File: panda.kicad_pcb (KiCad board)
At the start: 2 copper layers, 100 x 125 mm, 158 parts, among them J1 PIN6-9_Breakout, J10 Screw_Terminal_01x02, J11 24V_Lockout_Key_Switch, J12 XT60-M, J13 PT_1, J14 PT_4, J15 PT_2, J16 PT_5, J17 PT_3, J18 PT_6, J19 4-Pin Load Cell, J2 PIN10-13_Breakout, J20 5-Pin Load Cell, J21 Ignitor Screw Terminal, J3 Valve_1_PWR, J4 Valve_4_PWR, J5 Valve_2_PWR, J6 Valve_5_PWR, J7 Valve_3_PWR, J8 Valve_6_PWR, J9 Screw_Terminal_01x03, K1 G5Q-1A DC24, K2 G5Q-1A DC24, Q1 BSS138, Q2 BSS138, Q3 BSS138, Q4 BSS138, Q5 BSS138, Q6 BSS138, Q7 BSS138, Q8 BSS138, U1 ESP32-S3, U2 ADS112C04, U3 ADS112C04, U4 ADS112C04, U5 ADS112C04, U6 XC6206P332MR, U8 TPS5430DDA, U9 INA199A2DCK

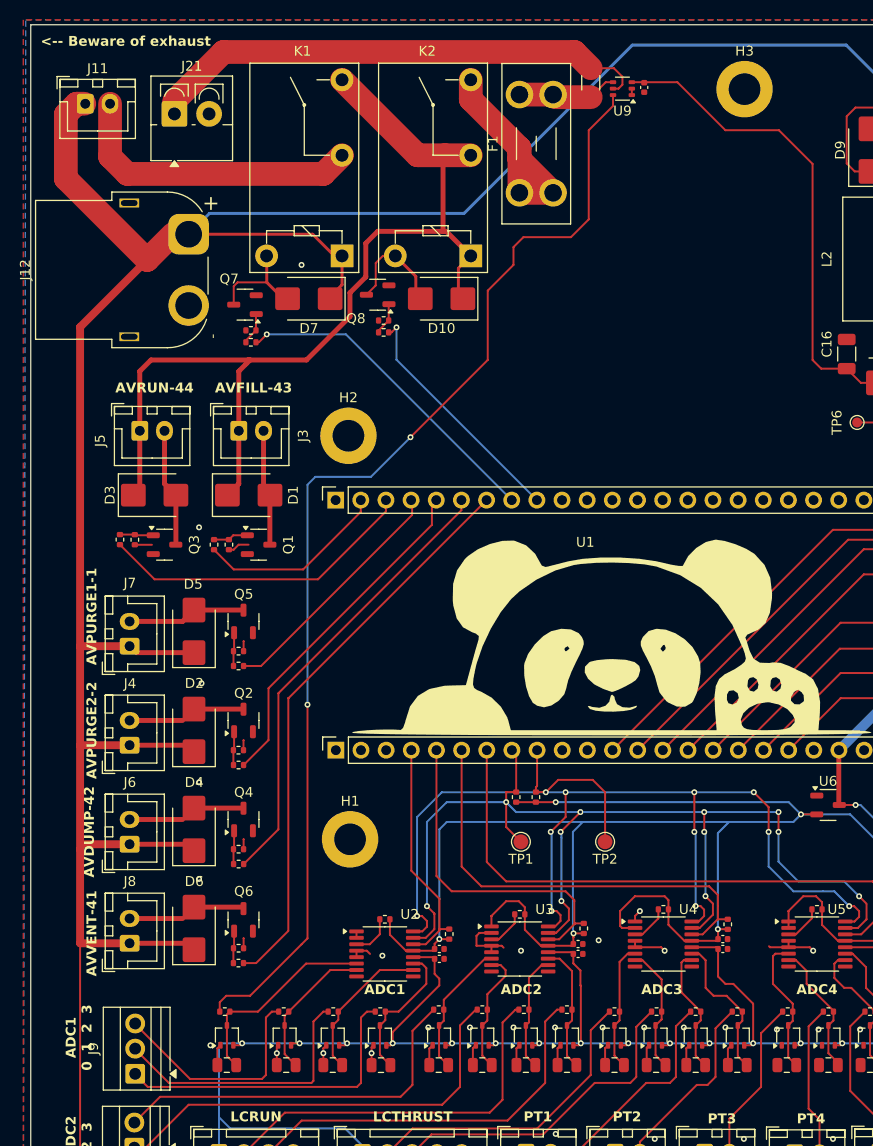
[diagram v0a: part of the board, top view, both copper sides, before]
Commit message: Add indicator LEDs and digital +24VSafe detection line
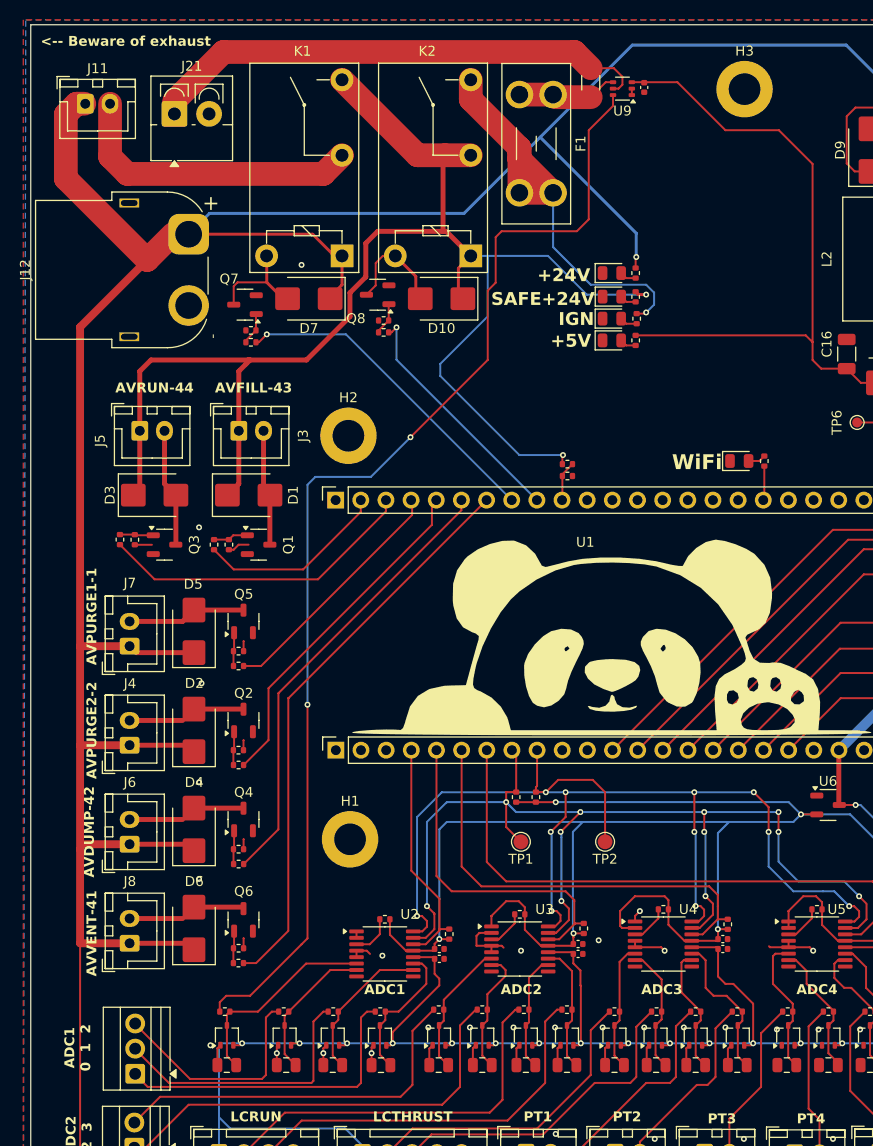
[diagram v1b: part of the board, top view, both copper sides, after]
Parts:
- added D11: LED-G, LED_SMD:LED_0805_2012Metric, F.Cu at (168.9, 56.6)
- added D12: LED-G, LED_SMD:LED_0805_2012Metric, F.Cu at (168.9, 49.8)
- added D13: LED-G, LED_SMD:LED_0805_2012Metric, F.Cu at (168.9, 52.2)
- added D14: LED-G, LED_SMD:LED_0805_2012Metric, F.Cu at (168.9, 54.4)
- added D8: LED-Y, LED_SMD:LED_0805_2012Metric, F.Cu at (181.8, 68.8)
- added R55: 1k, Resistor_SMD:R_0402_1005Metric, F.Cu at (184.3, 68.8)
- added R56: 1k, Resistor_SMD:R_0402_1005Metric, F.Cu at (171.3, 56.6)
- added R57: 22k, Resistor_SMD:R_0402_1005Metric, F.Cu at (171.3, 49.8)
- added R58: 22k, Resistor_SMD:R_0402_1005Metric, F.Cu at (171.3, 52.2)
- added R59: 22k, Resistor_SMD:R_0402_1005Metric, F.Cu at (171.4, 54.4)
- added R60: 270k, Resistor_SMD:R_0402_1005Metric, F.Cu at (164.4, 69.1)
- added R61: 33k, Resistor_SMD:R_0402_1005Metric, F.Cu at (164.4, 70.3)
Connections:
- net /Ignitor Control/IGNITOR_SOURCE renamed /Ignitor Control/IGNITOR_+VE
- net Net-(F1-Pad1) renamed /Ignitor Control/IGN_SUPPLY
- U1 pad 21: unconnected-(U1-GPIO21-Pad21) -> /ESP32 Breakout/WIFI_INDICATOR
- U1 pad 38: unconnected-(U1-GPIO38-Pad38) -> /ESP32 Breakout/+24V_SAFE_DETECT
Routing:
- net +24V_SAFE: track 100.0 -> 151.3 mm, vias 0 -> 2
- net /Ignitor Control/IGN_SUPPLY: track 22.8 -> 43.7 mm, vias 0 -> 1
- net +5V: track 320.5 -> 338.7 mm
- net +24V: track 422.0 -> 439.3 mm, vias 1 -> 2
- net /ESP32 Breakout/+24V_SAFE_DETECT: track 0.00 -> 4.07 mm
- net /ESP32 Breakout/WIFI_INDICATOR: track 0.00 -> 3.47 mm
- net Net-(D8-A): track 0.00 -> 1.80 mm
- net Net-(D14-A): track 0.00 -> 1.78 mm
- net Net-(D13-A): track 0.00 -> 1.68 mm
- net Net-(D11-A): track 0.00 -> 1.67 mm
- net Net-(D12-A): track 0.00 -> 1.67 mm
- net IGN_Current_Measurement: track 116.5 -> 118.1 mm
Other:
- board text added: "+24V"
- board text added: "+5V"
- board text added: "ADC1 0 1 2"
- board text added: "IGN"
- board text added: "SAFE+24V"
- board text added: "WiFi"
- board text added: "https://github.com/Queens-Rocket-Engineering-Team/prop-panda"
- board text removed: "ADC1 0 1 2 3"

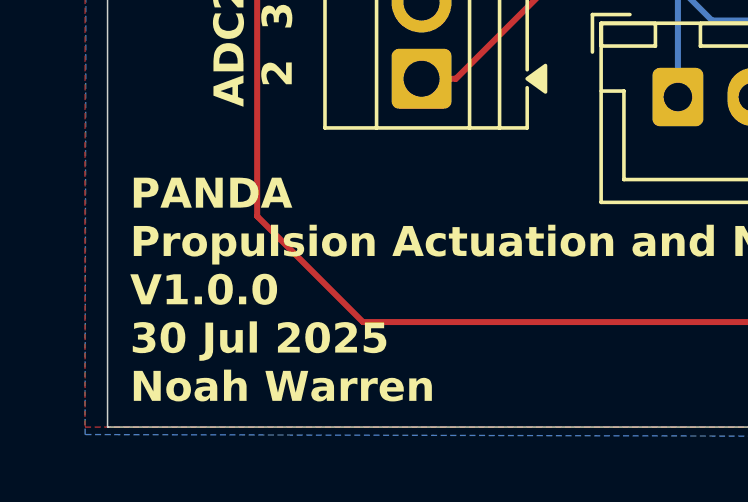
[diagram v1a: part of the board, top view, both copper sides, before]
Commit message: Update version numbers
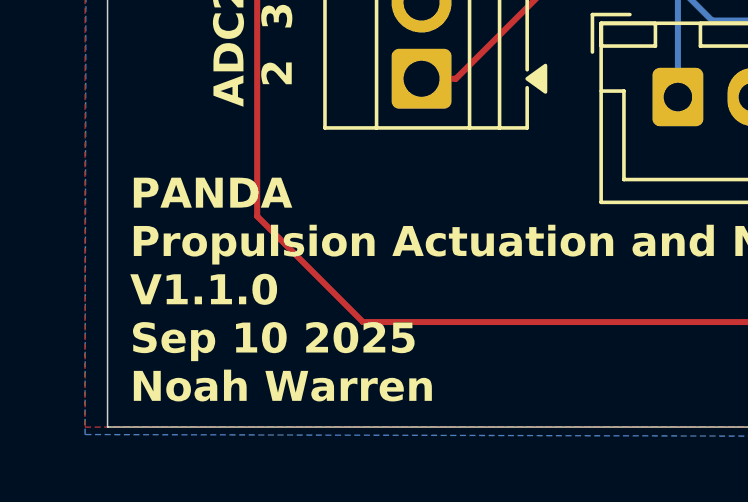
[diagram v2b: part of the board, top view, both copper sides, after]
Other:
- board text added: "PANDA Propulsion Actuation and Nominal Data Acquisition V1.1.0 Sep 10 2025 Noah Warren"
- board text removed: "PANDA Propulsion Actuation and Nominal Data Acquisition V1.0.0 30 Jul 2025 Noah Warren"
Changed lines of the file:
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@@
 	(title_block
 		(title "PANDA")
-		(rev "1.0.0")
+		(rev "1.1.0")
 		(company "Queen's Rocket Engineering Team")
-		(comment 1 "Propulsion Actuation and Nonsensical Data Acquisition")
+		(comment 1 "Propulsion Actuation and Nominal Data Acquisition")
 	)
 	(layers
@@
 		)
 	)
-	(gr_text "PANDA\nPropulsion Actuation and Nominal Data Acquisition\nV1.0.0\n30 Jul 2025\nNoah Warren"
+	(gr_text "PANDA\nPropulsion Actuation and Nominal Data Acquisition\nV1.1.0\nSep 10 2025\nNoah Warren"
 		(at 111 149 0)
 		(layer "F.SilkS")

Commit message: connected to GPIO pins
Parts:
- removed the U6 at (190.8, 103.5)
- added C1: 10uF, Capacitor_SMD:C_1206_3216Metric, F.Cu at (216.0, 92.0)
- added C15: 10uF, Capacitor_SMD:C_1206_3216Metric, F.Cu at (263.8, 51.6)
- added C16: 10uF, Capacitor_SMD:C_1206_3216Metric, F.Cu at (249.8, 59.5)
- added C18: 10uF, Capacitor_SMD:C_1206_3216Metric, F.Cu at (251.2, 54.5)
- added C2: 0.1μF, Capacitor_SMD:C_0402_1005Metric, F.Cu at (205.4, 93.4)
- added C20: 0.1μF, Capacitor_SMD:C_0402_1005Metric, F.Cu at (279.3, 45.2)
- added C3: 1μF, Capacitor_SMD:C_0402_1005Metric, F.Cu at (228.0, 87.5)
- added C4: 0.1μF, Capacitor_SMD:C_0402_1005Metric, F.Cu at (229.2, 90.0)
- added C5: 0.1μF, Capacitor_SMD:C_0402_1005Metric, F.Cu at (205.4, 99.3)
- added CR1: USBLC6-2SC6, Package_TO_SOT_SMD:SOT-23-6, F.Cu at (216.4, 71.5)
- added D11: 1N5819HW-7-F, Diode_SMD:D_SOD-123, F.Cu at (270.5, 77.1)
- added D12: 1N5819HW-7-F, Diode_SMD:D_SOD-123, F.Cu at (270.5, 82.8)
- added D14: LED-G, LED_SMD:LED_0805_2012Metric, F.Cu at (255.0, 60.0)
- added J1: USB_C_Receptacle_USB2.0_16P, Connector_USB:USB_C_Receptacle_HCTL_HC-TYPE-C-16P-01A, F.Cu at (225.0, 71.5)
- added R1: 0k, Resistor_SMD:R_0402_1005Metric, F.Cu at (202.0, 90.8)
- added R2: 10k, Resistor_SMD:R_0402_1005Metric, F.Cu at (202.5, 95.4)
- added R3: 5.1k, Resistor_SMD:R_0402_1005Metric, F.Cu at (219.2, 74.0)
- added R36: 680, Resistor_SMD:R_0402_1005Metric, F.Cu at (278.3, 37.2)
- added R4: 5.1k, Resistor_SMD:R_0402_1005Metric, F.Cu at (219.2, 69.0)
- added SW1: PTS636SM43SMTR LFS, Button_Switch_SMD:SW_Tactile_SPST_NO_Straight_CK_PTS636Sx25SMTRLFS, F.Cu at (195.8, 95.0)
- added SW2: PTS636SM43SMTR LFS, Button_Switch_SMD:SW_Tactile_SPST_NO_Straight_CK_PTS636Sx25SMTRLFS, F.Cu at (195.8, 100.2)
- added U7: XC6220B331PR-G, Package_TO_SOT_SMD:SOT-89-5, F.Cu at (260.6, 77.8)
- U1: value ESP32-S3 -> ESP32-S3-WROOM-1; footprint Library:ESP32_Devkit_C1_Noah -> RF_Module:ESP32-S3-WROOM-1
- moved G*** 127.9 mm to (41.1, 83.1)
- moved R8 76.2 mm to (239.2, 54.8)
- moved R9 75.9 mm to (239.2, 57.2)
- moved U1 60.1 mm to (216.2, 49.8), turned to 0 degrees
- moved C23 41.3 mm to (88.8, 132.3)
- moved C24 41.3 mm to (104.4, 132.3)
- moved C27 41.3 mm to (94.8, 132.3)
- moved D17 41.3 mm to (110.5, 54.9)
- moved D20 41.3 mm to (110.2, 129.3)
- moved H2 41.3 mm to (101.1, 68.8)
- moved Q2 41.3 mm to (90.5, 97.5)
- moved Q4 41.3 mm to (90.5, 107.5)
- moved Q5 41.3 mm to (90.5, 87.5)
- moved Q6 41.3 mm to (90.5, 117.6)
- moved R11 41.3 mm to (90.0, 102.0)
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- renumbered C5 to C10, C6 to C11, C7 to C12, C8 to C13, C10 to C14, C12 to C17, C14 to C19, C16 to C21, C29 to C22, C9 to C23, C13 to C24, C17 to C25, C18 to C26, C11 to C27, C15 to C28, C19 to C29, C20 to C30, C21 to C31, C22 to C32, C25 to C33, C26 to C34, C23 to C35, C24 to C36, C27 to C37, C28 to C38, C1 to C6, C2 to C7, C3 to C8, C4 to C9, D8 to D1, D7 to D10, D9 to D13, D11 to D15, D14 to D16, D10 to D17, D26 to D18, D28 to D19, D1 to D2, D34 to D20, D35 to D21, D27 to D22, D29 to D23, D36 to D24, D37 to D25, D30 to D26, D31 to D27, D38 to D28, D39 to D29, D2 to D3, D32 to D30, D33 to D31, D40 to D32, D41 to D33, D3 to D4, D4 to D5, D5 to D6, D6 to D7, D13 to D8, D12 to D9, J11 to J10, J12 to J11, J13 to J12, J14 to J13, J15 to J14, J16 to J15, J17 to J16, J18 to J17, J19 to J18, J20 to J19, J21 to J20, J9 to J21, J10 to J22, J1 to J3, J3 to J4, J4 to J5, J5 to J6, J6 to J7, J7 to J8, J8 to J9, L2 to L1, R3 to R10, R4 to R11, R5 to R12, R6 to R13, R7 to R14, R8 to R15, R9 to R16, R10 to R17, R11 to R18, R12 to R19, R13 to R20, R14 to R21, R15 to R22, R16 to R23, R17 to R24, R18 to R25, R19 to R26, R20 to R27, R21 to R28, R22 to R29, R23 to R30, R24 to R31, R58 to R32, R57 to R33, R25 to R34, R26 to R35, R29 to R37, R30 to R38, R56 to R39, R31 to R40, R32 to R41, R33 to R42, R34 to R43, R35 to R44, R36 to R45, R54 to R46, R59 to R47, R37 to R48, R38 to R49, R1 to R5, R53 to R50, R27 to R51, R28 to R52, R39 to R53, R40 to R54, R41 to R55, R42 to R56, R43 to R57, R44 to R58, R45 to R59, R2 to R6, R46 to R60, R47 to R61, R48 to R62, R49 to R63, R50 to R64, R51 to R65, R52 to R66, R55 to R7, R60 to R8, R61 to R9, TP3 to TP1, TP1 to TP2, TP2 to TP3, TP6 to TP4, U8 to U6, U9 to U8
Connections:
- net /ESP32 Breakout/WIFI_INDICATOR renamed WIFI_IND
- R8 pad 2: /ESP32 Breakout/+24V_SAFE_DETECT -> 24V_SAFE_DETECT
- R9 pad 1: /ESP32 Breakout/+24V_SAFE_DETECT -> 24V_SAFE_DETECT
- U1 pad 1: VALVE_3_CTL -> GND
- U1 pad 10: /ESP32 Breakout/PIN10_BREAKOUT -> VALVE_4_CTL
- U1 pad 11: /ESP32 Breakout/PIN11_BREAKOUT -> VALVE_5_CTL
- U1 pad 12: /ESP32 Breakout/PIN12_BREAKOUT -> VALVE_6_CTL
- U1 pad 13: /ESP32 Breakout/PIN13_BREAKOUT -> USB_N
- U1 pad 14: unconnected-(U1-GPIO14-Pad14) -> USB_P
- U1 pad 15: I2C_SDA -> I2C_SCL
- U1 pad 16: I2C_SCL -> I2C_SDA
- U1 pad 17: unconnected-(U1-GPIO17-Pad17) -> I2C_DRDY_ADC1
- U1 pad 18: unconnected-(U1-GPIO18-Pad18) -> I2C_DRDY_ADC2
- U1 pad 19: unconnected-(U1-GPIO19/USB_D--Pad19) -> I2C_DRDY_ADC3
- U1 pad 2: VALVE_4_CTL -> +3.3V
- U1 pad 20: unconnected-(U1-GPIO20/USB_D+-Pad20) -> I2C_DRDY_ADC4
- U1 pad 3: /ESP32 Breakout/PIN3_BREAKOUT -> RESET
- U1 pad 35: (no net) -> unconnected-(U1-IO42-Pad35)
- U1 pad 36: (no net) -> unconnected-(U1-RXD0-Pad36)
- U1 pad 37: (no net) -> unconnected-(U1-TXD0-Pad37)
- U1 pad 38: /ESP32 Breakout/+24V_SAFE_DETECT -> unconnected-(U1-IO2-Pad38)
- U1 pad 39: IGNITOR_CTL -> unconnected-(U1-IO1-Pad39)
- U1 pad 4: I2C_DRDY_ADC1 -> IGNITOR_CTL
- U1 pad 40: SAFE_24V_CTL -> GND
- U1 pad 41: VALVE_6_CTL -> GND
- U1 pad 5: I2C_DRDY_ADC2 -> SAFE_24V_CTL
- U1 pad 6: I2C_DRDY_ADC3 -> 24V_SAFE_DETECT
- U1 pad 7: I2C_DRDY_ADC4 -> VALVE_2_CTL
- U1 pad 8: /ESP32 Breakout/PIN8_BREAKOUT -> VALVE_1_CTL
- U1 pad 9: /ESP32 Breakout/PIN9_BREAKOUT -> VALVE_3_CTL
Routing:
- net Net-(CR1-Pad3): track 0.00 -> 7.16 mm
- net 5V_USB: track 0.00 -> 7.01 mm
- net Net-(CR1-Pad1): track 0.00 -> 6.53 mm
- net /ESP32 Breakout/+24V_SAFE_DETECT: track 4.07 -> 0.00 mm
- net WIFI_IND: track 3.47 -> 0.00 mm
- net Net-(J1-CC1): track 0.00 -> 2.31 mm
- net Net-(J1-CC2): track 0.00 -> 2.11 mm
- net Net-(D1-A): track 1.80 -> 0.00 mm
- net +24V_SAFE: track 151.3 -> 150.4 mm, vias 2 -> 1

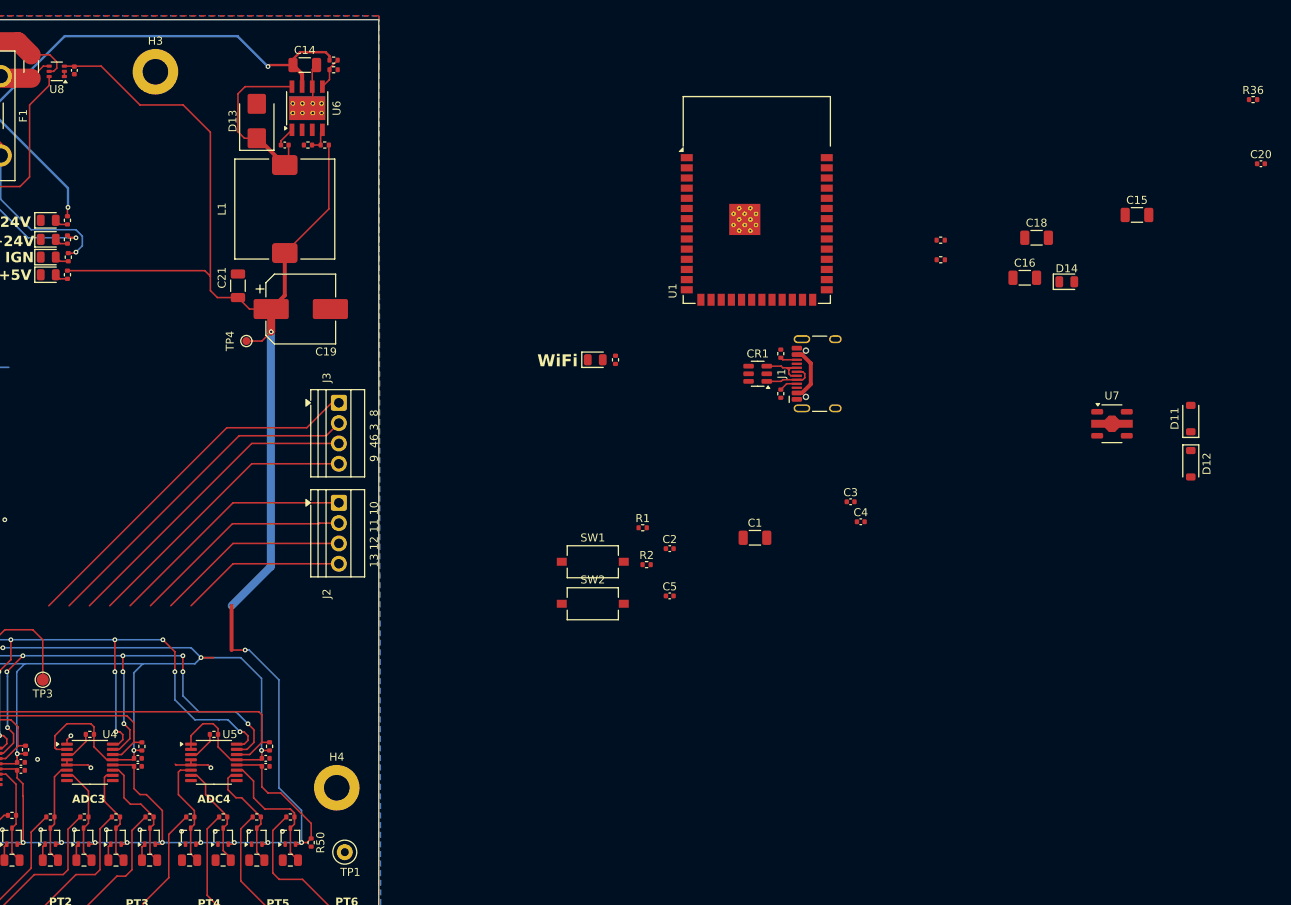
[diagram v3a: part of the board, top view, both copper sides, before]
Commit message: added 24V lockout key LED indicator
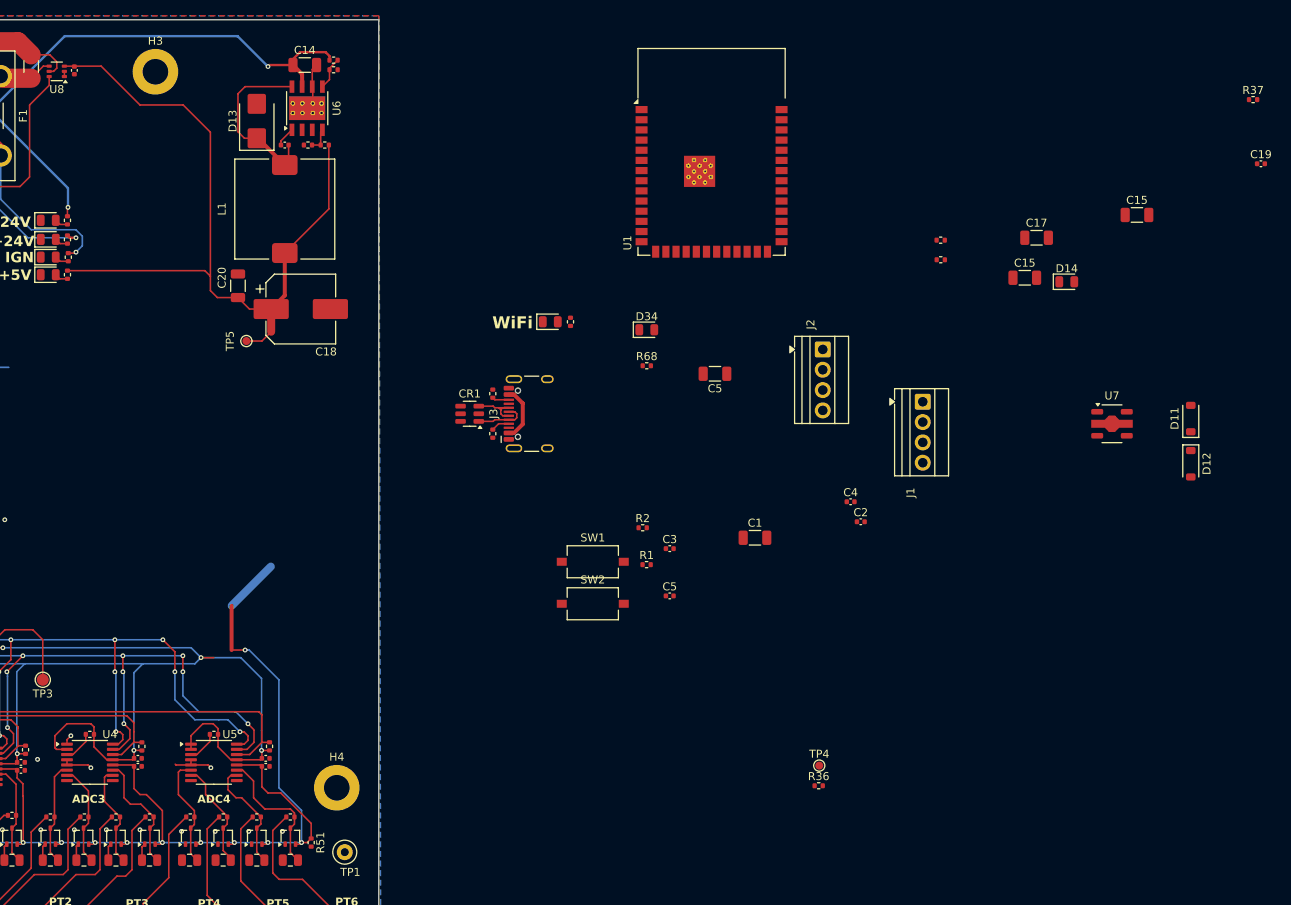
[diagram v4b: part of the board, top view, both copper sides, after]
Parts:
- added C5: 10uF, Capacitor_SMD:C_1206_3216Metric, F.Cu at (211.0, 71.5)
- added D34: LED-G, LED_SMD:LED_0805_2012Metric, F.Cu at (202.5, 66.0)
- added R36: 100k, Resistor_SMD:R_0402_1005Metric, F.Cu at (224.0, 123.0)
- added R68: 22k, Resistor_SMD:R_0402_1005Metric, F.Cu at (202.5, 70.5)
- added TP4: TP_+3.3V, TestPoint:TestPoint_Pad_D1.0mm, F.Cu at (224.1, 120.5)
- C1: value 10uF -> 22uF
- moved J1 74.1 mm to (237.0, 75.0)
- moved J2 60.9 mm to (224.5, 68.5)
- moved CR1 36.3 mm to (180.4, 76.5)
- moved J3 36.3 mm to (189.0, 76.5)
- moved R5 36.3 mm to (183.2, 79.0)
- moved R6 36.3 mm to (183.2, 74.0)
- moved U1 8.25 mm to (210.6, 43.7)
- moved D1 7.36 mm to (190.4, 65.0)
- moved R7 7.36 mm to (193.0, 65.0)
- renumbered C16 to C15, C17 to C16, C18 to C17, C19 to C18, C20 to C19, C4 to C2, C21 to C20, C22 to C21, C23 to C22, C24 to C23, C25 to C24, C26 to C25, C27 to C26, C28 to C27, C29 to C28, C30 to C29, C2 to C3, C31 to C30, C32 to C31, C33 to C32, C34 to C33, C35 to C34, C36 to C35, C37 to C36, C38 to C37, C3 to C4, J2 to J1, J3 to J2, J1 to J3, R2 to R1, R1 to R2, R5 to R3, R36 to R37, R37 to R38, R38 to R39, R6 to R4, R39 to R40, R40 to R41, R41 to R42, R42 to R43, R43 to R44, R44 to R45, R45 to R46, R46 to R47, R47 to R48, R48 to R49, R3 to R5, R49 to R50, R50 to R51, R51 to R52, R52 to R53, R53 to R54, R54 to R55, R55 to R56, R56 to R57, R57 to R58, R58 to R59, R4 to R6, R59 to R60, R60 to R61, R61 to R62, R62 to R63, R63 to R64, R64 to R65, R65 to R66, R66 to R67, TP4 to TP5
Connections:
- J1 pad 1: /ESP32 Breakout/PIN10_BREAKOUT -> unconnected-(J1-Pin_1-Pad1)
- J1 pad 2: /ESP32 Breakout/PIN11_BREAKOUT -> unconnected-(J1-Pin_2-Pad2)
- J1 pad 3: /ESP32 Breakout/PIN12_BREAKOUT -> unconnected-(J1-Pin_3-Pad3)
- J1 pad 4: /ESP32 Breakout/PIN13_BREAKOUT -> unconnected-(J1-Pin_4-Pad4)
- J2 pad 1: /ESP32 Breakout/PIN8_BREAKOUT -> unconnected-(J2-Pin_1-Pad1)
- J2 pad 2: /ESP32 Breakout/PIN3_BREAKOUT -> unconnected-(J2-Pin_2-Pad2)
- J2 pad 3: /ESP32 Breakout/PIN46_BREAKOUT -> unconnected-(J2-Pin_3-Pad3)
- J2 pad 4: /ESP32 Breakout/PIN9_BREAKOUT -> unconnected-(J2-Pin_4-Pad4)
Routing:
- net /ESP32 Breakout/PIN8_BREAKOUT: track 46.8 -> 0.00 mm
- net /ESP32 Breakout/PIN3_BREAKOUT: track 43.2 -> 0.00 mm
- net /ESP32 Breakout/PIN46_BREAKOUT: track 39.6 -> 0.00 mm
- net /ESP32 Breakout/PIN9_BREAKOUT: track 36.0 -> 0.00 mm
- net /ESP32 Breakout/PIN10_BREAKOUT: track 31.4 -> 0.00 mm
- net +5V: track 338.7 -> 309.3 mm, vias 18 -> 17
- net /ESP32 Breakout/PIN11_BREAKOUT: track 27.8 -> 0.00 mm
- net /ESP32 Breakout/PIN12_BREAKOUT: track 24.2 -> 0.00 mm
- net /ESP32 Breakout/PIN13_BREAKOUT: track 20.7 -> 0.00 mm
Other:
- board text removed: "13 12 11 10"
- board text removed: "9 46 3 8"
